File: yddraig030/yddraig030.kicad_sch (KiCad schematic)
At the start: 0 parts

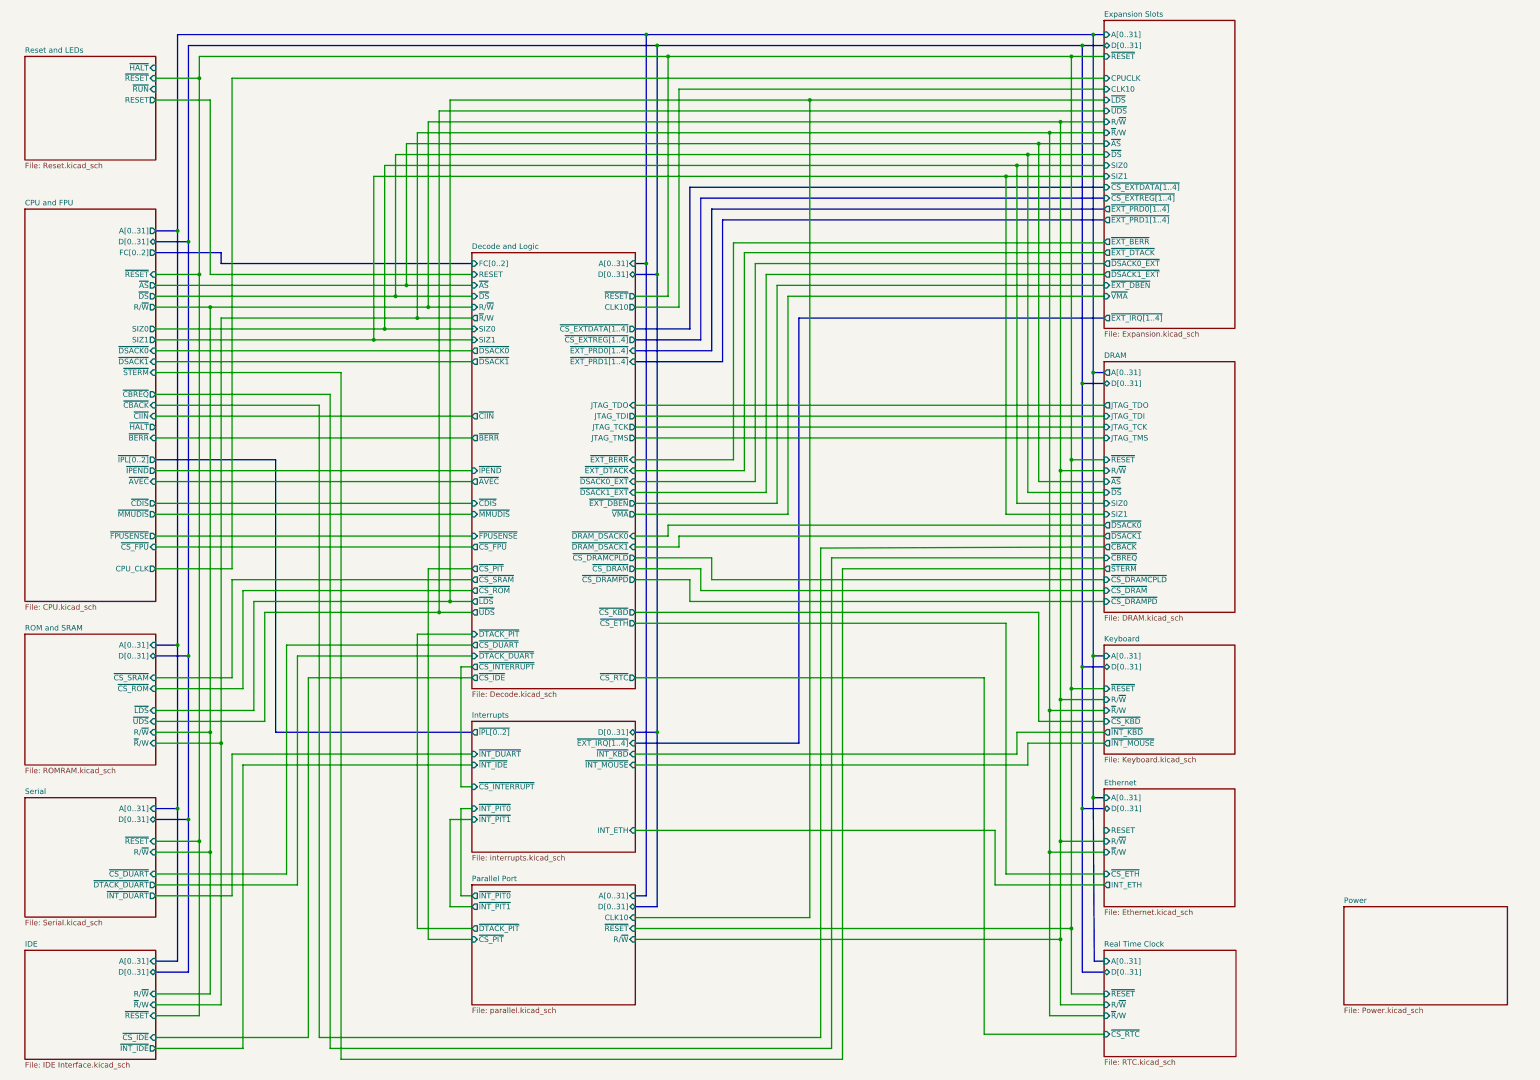
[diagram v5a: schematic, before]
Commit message: yddraig030: Fixed ERC check errors
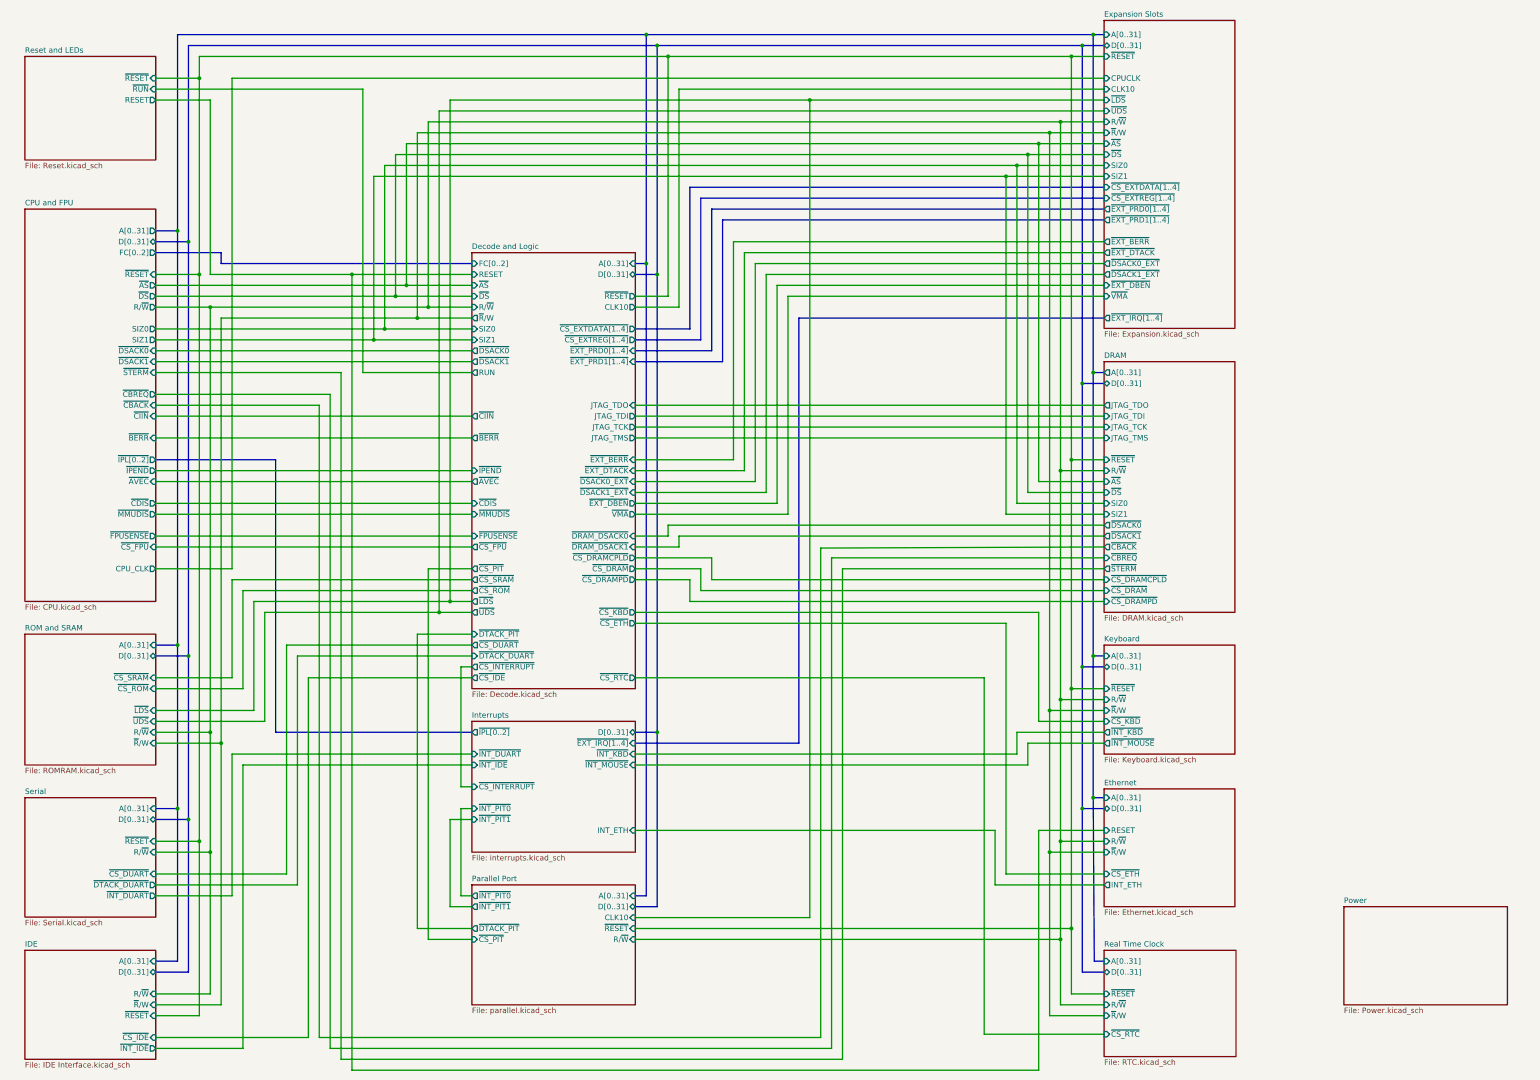
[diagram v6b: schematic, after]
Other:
- sheet CPU and FPU ports: added none; removed ~{HALT}
- sheet Decode and Logic ports: added RUN; removed none
- sheet Reset and LEDs ports: added none; removed ~{HALT}
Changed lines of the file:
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@@
   (junction (at 177.8 73.66) (diameter 0) (color 0 0 0 0)
   )
+  (junction (at 109.22 76.2) (diameter 0) (color 0 0 0 0)
+  )
   (junction (at 116.84 88.9) (diameter 0) (color 0 0 0 0)
   )
@@
     (stroke (width 0) (type default) (color 0 0 0 0))
   )
+  (wire (pts (xy 269.24 205.74) (xy 284.48 205.74))
+    (stroke (width 0) (type default) (color 0 0 0 0))
+  )
   (wire (pts (xy 114.3 91.44) (xy 137.414 91.44))
     (stroke (width 0) (type default) (color 0 0 0 0))
@@
     (stroke (width 0) (type default) (color 0 0 0 0))
   )
+  (wire (pts (xy 109.22 261.62) (xy 269.24 261.62))
+    (stroke (width 0) (type default) (color 0 0 0 0))
+  )
   (wire (pts (xy 284.48 132.08) (xy 261.62 132.08))
     (stroke (width 0) (type default) (color 0 0 0 0))
@@
     (stroke (width 0) (type default) (color 0 0 0 0))
   )
-  (wire (pts (xy 198.12 68.834) (xy 198.12 119.38))
+  (wire (pts (xy 198.12 68.58) (xy 198.12 119.38))
     (stroke (width 0) (type default) (color 0 0 0 0))
   )
@@
     (stroke (width 0) (type default) (color 0 0 0 0))
   )
+  (wire (pts (xy 109.22 76.2) (xy 109.22 261.62))
+    (stroke (width 0) (type default) (color 0 0 0 0))
+  )
   (wire (pts (xy 200.66 121.92) (xy 200.66 71.12))
     (stroke (width 0) (type default) (color 0 0 0 0))
@@
     (stroke (width 0) (type default) (color 0 0 0 0))
   )
+  (wire (pts (xy 109.22 76.2) (xy 76.2 76.2))
+    (stroke (width 0) (type default) (color 0 0 0 0))
+  )
   (bus (pts (xy 78.74 73.66) (xy 78.74 71.12))
     (stroke (width 0) (type default) (color 0 0 0 0))
   )
-  (wire (pts (xy 284.48 68.834) (xy 198.12 68.834))
+  (wire (pts (xy 284.48 68.58) (xy 198.12 68.58))
     (stroke (width 0) (type default) (color 0 0 0 0))
   )
@@
     (stroke (width 0) (type default) (color 0 0 0 0))
   )
+  (wire (pts (xy 111.76 99.06) (xy 111.76 33.02))
+    (stroke (width 0) (type default) (color 0 0 0 0))
+  )
   (wire (pts (xy 284.48 139.7) (xy 218.44 139.954))
     (stroke (width 0) (type default) (color 0 0 0 0))
@@
     (stroke (width 0) (type default) (color 0 0 0 0))
   )
-  (wire (pts (xy 137.16 76.2) (xy 76.2 76.2))
+  (wire (pts (xy 137.16 76.2) (xy 109.22 76.2))
     (stroke (width 0) (type default) (color 0 0 0 0))
   )
@@
     (stroke (width 0) (type default) (color 0 0 0 0))
   )
+  (wire (pts (xy 137.16 99.06) (xy 111.76 99.06))
+    (stroke (width 0) (type default) (color 0 0 0 0))
+  )
   (wire (pts (xy 274.32 231.14) (xy 274.32 246.38))
     (stroke (width 0) (type default) (color 0 0 0 0))
@@
     (stroke (width 0) (type default) (color 0 0 0 0))
   )
+  (wire (pts (xy 269.24 261.62) (xy 269.24 205.74))
+    (stroke (width 0) (type default) (color 0 0 0 0))
+  )
   (wire (pts (xy 203.2 73.66) (xy 284.48 73.66))
     (stroke (width 0) (type default) (color 0 0 0 0))
@@
     (stroke (width 0) (type default) (color 0 0 0 0))
   )
+  (wire (pts (xy 111.76 33.02) (xy 63.5 33.02))
+    (stroke (width 0) (type default) (color 0 0 0 0))
+  )
   (wire (pts (xy 284.48 218.44) (xy 259.08 218.44))
     (stroke (width 0) (type default) (color 0 0 0 0))
@@
       (effects (font (size 1.27 1.27)) (justify right))
     )
-    (pin "~{HALT}" output (at 63.5 111.76 0)
-      (effects (font (size 1.27 1.27)) (justify right))
-    )
     (pin "~{CIIN}" input (at 63.5 109.22 0)
       (effects (font (size 1.27 1.27)) (justify right))
@@
       (effects (font (size 1.27 1.27)) (justify left))
     )
+    (pin "RUN" output (at 137.16 99.06 180)
+      (effects (font (size 1.27 1.27)) (justify left))
+    )
   )
   (sheet (at 284.48 196.088) (size 30.48 27.432) (fields_autoplaced)
@@
       (effects (font (size 1.27 1.27)) (justify left top))
     )
-    (pin "~{HALT}" input (at 63.5 28.067 0)
-      (effects (font (size 1.27 1.27)) (justify right))
-    )
     (pin "~{RESET}" input (at 63.5 30.48 0)
       (effects (font (size 1.27 1.27)) (justify right))
@@
       (reference "#PWR0203") (unit 1) (value "GND") (footprint "")
     )
-    (path "/00000000-0000-0000-0000-00006147db65/00000000-0000-0000-0000-000061487a45"
-      (reference "#PWR0204") (unit 1) (value "+5V") (footprint "")
-    )
-    (path "/00000000-0000-0000-0000-00006147db65/00000000-0000-0000-0000-000061487a3f"
-      (reference "#PWR0205") (unit 1) (value "GND") (footprint "")
-    )
     (path "/00000000-0000-0000-0000-00006147db65/00000000-0000-0000-0000-0000614879ce"
       (reference "#PWR0206") (unit 1) (value "+5V") (footprint "")
@@
       (reference "D201") (unit 1) (value "RED") (footprint "LED_THT:LED_D5.0mm")
     )
-    (path "/00000000-0000-0000-0000-00006147db65/00000000-0000-0000-0000-000061487a39"
-      (reference "D202") (unit 1) (value "RED") (footprint "LED_THT:LED_D5.0mm")
-    )
     (path "/00000000-0000-0000-0000-00006147db65/00000000-0000-0000-0000-000061487a62"
       (reference "D203") (unit 1) (value "GREEN") (footprint "LED_THT:LED_D5.0mm")
@@
       (reference "Q201") (unit 1) (value "2N4403") (footprint "Package_TO_SOT_THT:TO-92")
     )
-    (path "/00000000-0000-0000-0000-00006147db65/00000000-0000-0000-0000-000061487a33"
-      (reference "Q202") (unit 1) (value "2N4403") (footprint "Package_TO_SOT_THT:TO-92")
-    )
     (path "/00000000-0000-0000-0000-00006147db65/00000000-0000-0000-0000-000061487a5c"
       (reference "Q203") (unit 1) (value "2N4403") (footprint "Package_TO_SOT_THT:TO-92")
@@
       (reference "R203") (unit 1) (value "10K") (footprint "Resistor_THT:R_Axial_DIN0207_L6.3mm_D2.5mm_P10.16mm_Horizontal")
     )
-    (path "/00000000-0000-0000-0000-00006147db65/00000000-0000-0000-0000-000061487a27"
-      (reference "R204") (unit 1) (value "1K") (footprint "Resistor_THT:R_Axial_DIN0207_L6.3mm_D2.5mm_P10.16mm_Horizontal")
-    )
-    (path "/00000000-0000-0000-0000-00006147db65/00000000-0000-0000-0000-000061487a2d"
-      (reference "R205") (unit 1) (value "150R") (footprint "Resistor_THT:R_Axial_DIN0207_L6.3mm_D2.5mm_P10.16mm_Horizontal")
-    )
     (path "/00000000-0000-0000-0000-00006147db65/00000000-0000-0000-0000-00006148799e"
       (reference "R206") (unit 1) (value "38K") (footprint "Resistor_THT:R_Axial_DIN0207_L6.3mm_D2.5mm_P10.16mm_Horizontal")
@@
     )
     (path "/00000000-0000-0000-0000-000061478359/7458f684-f745-4677-9f01-a8e13c0d930b"
-      (reference "U402") (unit 1) (value "AS6C4008-55PCN") (footprint "Package_DIP:DIP-32_W15.24mm_Socket")
+      (reference "U402") (unit 1) (value "AS6C4008-55PCN") (footprint "Package_DIP:DIP-32_W15.24mm")
     )
     (path "/00000000-0000-0000-0000-000061478359/ba78d98f-a84d-4337-b33e-2b4c0120d6e3"
@@
     )
     (path "/00000000-0000-0000-0000-000061478359/f0b710d4-956c-4ebf-a7f7-609dc88b46c5"
-      (reference "U404") (unit 1) (value "AS6C4008-55PCN") (footprint "Package_DIP:DIP-32_W15.24mm_Socket")
+      (reference "U404") (unit 1) (value "AS6C4008-55PCN") (footprint "Package_DIP:DIP-32_W15.24mm")
     )
     (path "/00000000-0000-0000-0000-000061478359/af61db1d-0a94-4818-8efc-99f46467ee03"

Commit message: Started PCB layout
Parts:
- added H101, H102, H103, H104, H105, H106: MountingHole, MountingHole:MountingHole_4.3mm_M4, symbol Mechanical:MountingHole
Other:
- sheet Decode and Logic ports: added INT_ETH, ~{INT_ETH}; removed none
- sheet Interrupts ports: added ~{INT_ETH}; removed INT_ETH

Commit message: More changes in yddraig030 layout
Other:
- removed sheet Parallel Port
- sheet Decode and Logic ports: added none; removed ~{CS_PIT}, ~{CS_SRAM}, ~{DTACK_PIT}
- sheet Interrupts ports: added none; removed ~{INT_PIT0}, ~{INT_PIT1}
- sheet ROM and SRAM ports: added none; removed ~{CS_SRAM}
